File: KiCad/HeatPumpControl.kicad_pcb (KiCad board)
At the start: 2 copper layers, 34.3 x 40.9 mm, 34 parts, among them J1 Conn_01x04_Male, J2 Conn_01x04_Male, J3 Conn_01x04_Male, Q1 2N2222A, U1 TSOP23xx, U2 SeedStudio XIAO ESP32 C3 v1

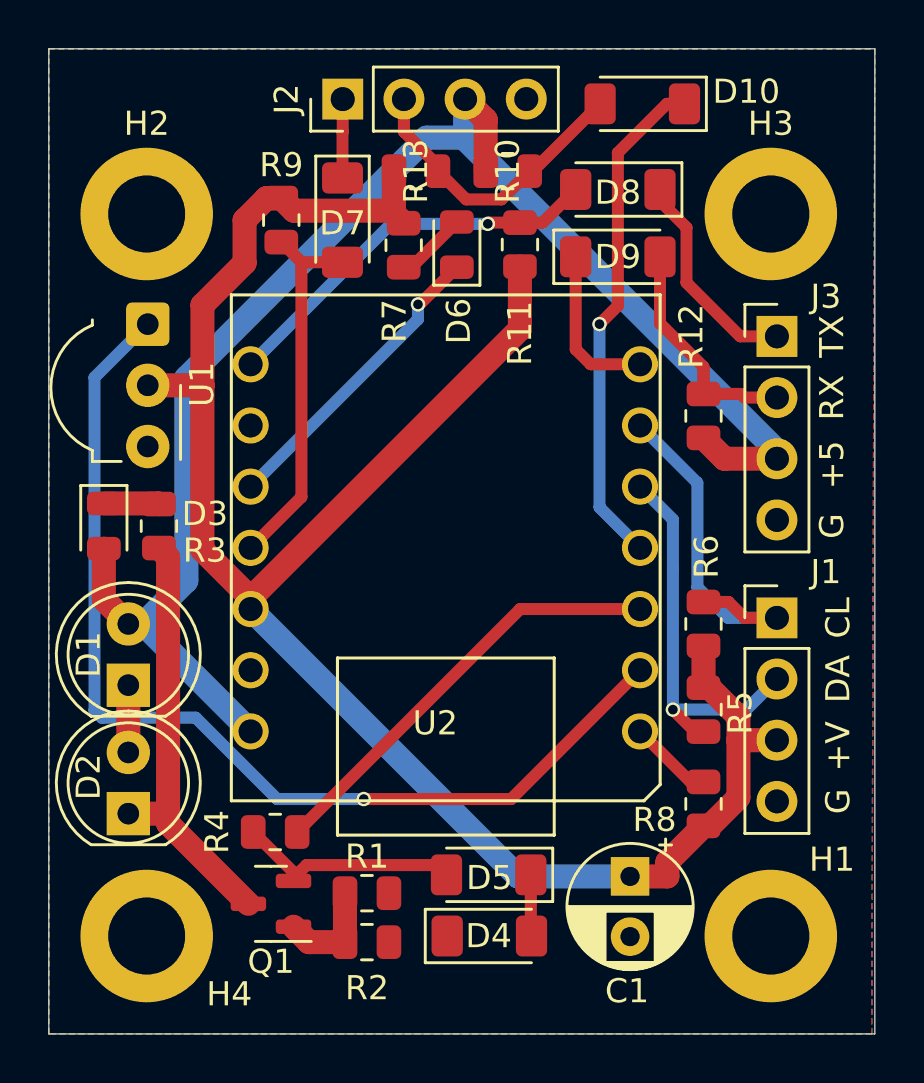
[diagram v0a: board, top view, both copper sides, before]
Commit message: Fixed Q1 pinout and grounding fills
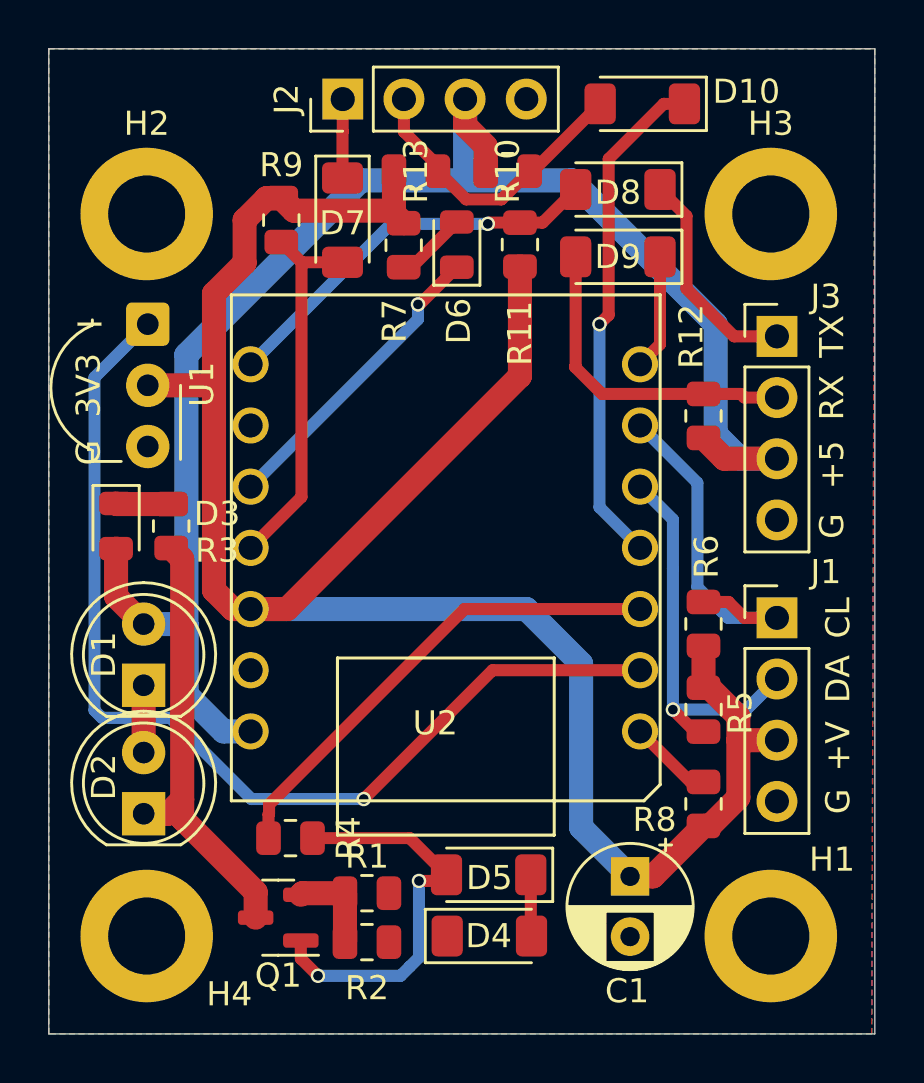
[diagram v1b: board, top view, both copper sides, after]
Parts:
- R1, R2: value 10 -> 27
- R3: value 1.8k -> 470
- R7: value 4k7 -> 430
- moved R4 0.68 mm to (145.9, 134.7), turned to 0 degrees
- moved Q1 0.65 mm to (145.4, 138.0)
- moved D1 0.64 mm to (139.8, 128.4)
- moved D2 0.64 mm to (139.8, 133.7)
- moved D3 0.51 mm to (138.7, 121.8)
- moved R3 0.51 mm to (141.0, 121.8)
- turned D9 to 180 degrees
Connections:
- net Net-(D10-K) renamed /GPIO5
- net Net-(D6-K) renamed /GPIO9
- net Net-(D7-A) renamed /GPIO10
- net Net-(U1-OUT) renamed /GPIO3
- net Net-(U2-IO4/A2/D2) renamed /GPIO4
- D8 pad 1: /TX -> Net-(D8-K)
- D8 pad 2: Net-(D8-A) -> /RX
- D9 pad 1: Net-(D9-K) -> /TX
- D9 pad 2: /RX -> Net-(D9-A)
- J3 pad 1: /TX -> Net-(D8-K)
- J3 pad 2: /RX -> Net-(D9-A)
- Q1 pad 1: /LED1 -> Net-(D4-A)
- Q1 pad 2: Net-(D4-A) -> /LED1
- R11 pad 2: Net-(D8-A) -> /RX
- R12 pad 2: /RX -> Net-(D9-A)
- U2 pad 7: Net-(D9-K) -> /TX
- U2 pad 8: Net-(D8-A) -> /RX
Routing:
- net Net-(D8-A): track 16.5 -> 0.00 mm, vias 1 -> 0
- net Net-(D9-A): track 0.00 -> 13.5 mm
- net Net-(D8-K): track 0.00 -> 9.15 mm
- net Net-(D4-A): track 9.40 -> 16.9 mm, vias 0 -> 2
- net /RX: track 9.55 -> 16.5 mm, vias 0 -> 1
- net Net-(D9-K): track 6.77 -> 0.00 mm
- net +5V: track 64.2 -> 70.8 mm
- net +3V3: track 82.7 -> 88.2 mm
- net /TX: track 9.00 -> 4.80 mm
- net /GPIO4: track 18.1 -> 20.2 mm
- net /LED2: track 18.0 -> 18.6 mm
- net /LED1: track 4.43 -> 3.89 mm
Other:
- board text added: "3V3"
- board text added: "Heat pump controller rev 2.0.1 (C) 2023 - Hans Rune Bue <email@hansrune.net>"
- board text removed: "Heat pump controller rev 2.0 (C) 2023 - Hans Rune Bue <email@hansrune.net>"

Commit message: v2.0.1 KiCAD changes
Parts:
- turned D9 to 0 degrees
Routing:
- net Net-(D9-A): track 13.5 -> 9.55 mm
- net /TX: track 4.80 -> 6.40 mm
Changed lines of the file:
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@@
 		)
 		(property "Value" "1.2k"
-			(at 0 1.65 360)
+			(at 0 1.65 0)
 			(layer "F.Fab")
 			(effects
@@
 		)
 		(property "Footprint" "Resistor_SMD:R_0805_2012Metric"
-			(at 0 0 360)
+			(at 0 0 0)
 			(layer "F.Fab")
 			(hide yes)
@@
 		)
 		(property "Datasheet" ""
-			(at 0 0 360)
+			(at 0 0 0)
 			(layer "F.Fab")
 			(hide yes)
@@
 		)
 		(property "Description" ""
-			(at 0 0 360)
+			(at 0 0 0)
 			(layer "F.Fab")
 			(hide yes)
@@
 		)
 		(fp_text user "${REFERENCE}"
-			(at 0 0 360)
+			(at 0 0 0)
 			(layer "F.Fab")
 			(effects
@@
 	(footprint "Diode_SMD:D_MiniMELF"
 		(layer "F.Cu")
-		(at 159.512 110.617 180)
+		(at 159.512 110.617)
 		(descr "Diode Mini-MELF (SOD-80)")
 		(tags "Diode Mini-MELF (SOD-80)")
@@
 		(attr smd)
 		(fp_line
-			(start 1.75 -1.11)
-			(end -2.66 -1.11)
+			(start -2.66 -1.11)
+			(end -2.66 1.11)
 			(stroke
 				(width 0.12)
@@
 		)
 		(fp_line
-			(start -2.66 -1.11)
-			(end -2.66 1.11)
+			(start 1.75 -1.11)
+			(end -2.66 -1.11)
 			(stroke
 				(width 0.12)
@@
 		)
 		(fp_line
-			(start 2.65 1.1)
-			(end -2.65 1.1)
+			(start -2.65 -1.1)
+			(end 2.65 -1.1)
 			(stroke
 				(width 0.05)
@@
 		)
 		(fp_line
-			(start 2.65 -1.1)
-			(end 2.65 1.1)
+			(start -2.65 1.1)
+			(end -2.65 -1.1)
 			(stroke
 				(width 0.05)
@@
 		)
 		(fp_line
-			(start -2.65 1.1)
-			(end -2.65 -1.1)
+			(start 2.65 -1.1)
+			(end 2.65 1.1)
 			(stroke
 				(width 0.05)
@@
 		)
 		(fp_line
-			(start -2.65 -1.1)
-			(end 2.65 -1.1)
+			(start 2.65 1.1)
+			(end -2.65 1.1)
 			(stroke
 				(width 0.05)
@@
 		)
 		(fp_line
-			(start 1.65 0.8)
-			(end -1.65 0.8)
+			(start -1.65 -0.8)
+			(end 1.65 -0.8)
 			(stroke
 				(width 0.1)
@@
 		)
 		(fp_line
-			(start 1.65 -0.8)
-			(end 1.65 0.8)
+			(start -1.65 0.8)
+			(end -1.65 -0.8)
 			(stroke
 				(width 0.1)
@@
 		)
 		(fp_line
-			(start 0.25 0.4)
+			(start -0.75 0)
 			(end -0.35 0)
 			(stroke
@@
 		)
 		(fp_line
-			(start 0.25 0)
-			(end 0.75 0)
+			(start -0.35 0)
+			(end -0.35 -0.55)
 			(stroke
 				(width 0.1)
@@
 		)
 		(fp_line
-			(start 0.25 -0.4)
-			(end 0.25 0.4)
+			(start -0.35 0)
+			(end -0.35 0.55)
 			(stroke
 				(width 0.1)
@@
 		)
 		(fp_line
-			(start -0.35 0)
-			(end -0.35 0.55)
+			(start 0.25 -0.4)
+			(end 0.25 0.4)
 			(stroke
 				(width 0.1)
@@
 		)
 		(fp_line
-			(start -0.35 0)
-			(end -0.35 -0.55)
+			(start 0.25 0)
+			(end 0.75 0)
 			(stroke
 				(width 0.1)
@@
 		)
 		(fp_line
-			(start -0.75 0)
+			(start 0.25 0.4)
 			(end -0.35 0)
 			(stroke
@@
 		)
 		(fp_line
-			(start -1.65 0.8)
-			(end -1.65 -0.8)
+			(start 1.65 -0.8)
+			(end 1.65 0.8)
 			(stroke
 				(width 0.1)
@@
 		)
 		(fp_line
-			(start -1.65 -0.8)
-			(end 1.65 -0.8)
+			(start 1.65 0.8)
+			(end -1.65 0.8)
 			(stroke
 				(width 0.1)
@@
 		)
 		(pad "1" smd roundrect
-			(at -1.75 0 180)
+			(at -1.75 0)
 			(size 1.3 1.7)
 			(layers "F.Cu" "F.Paste" "F.Mask")
@@
 		)
 		(pad "2" smd roundrect
-			(at 1.75 0 180)
+			(at 1.75 0)
 			(size 1.3 1.7)
 			(layers "F.Cu" "F.Paste" "F.Mask")
@@
 	)
 	(segment
-		(start 161.262 114.249)
+		(start 159.0197 115.0777)
 		(end 160.4333 115.0777)
 		(width 0.5)
@@
 	)
 	(segment
-		(start 161.262 110.617)
-		(end 161.262 114.249)
+		(start 157.762 113.82)
+		(end 159.0197 115.0777)
+		(width 0.5)
+		(layer "F.Cu")
+		(net 17)
+	)
+	(segment
+		(start 157.762 110.617)
+		(end 157.762 113.82)
 		(width 0.5)
 		(layer "F.Cu")
@@
 	)
 	(segment
-		(start 157.762 115.161)
-		(end 157.762 110.617)
+		(start 166.116 116.459)
+		(end 164.766 116.459)
 		(width 0.5)
 		(layer "F.Cu")
@@
 	)
 	(segment
-		(start 163.068 116.3085)
-		(end 158.8535 116.3085)
+		(start 161.262 112.113)
+		(end 163.068 113.919)
 		(width 0.5)
 		(layer "F.Cu")
@@
 	)
 	(segment
-		(start 166.116 116.459)
-		(end 164.766 116.459)
+		(start 163.068 113.919)
+		(end 163.068 116.3085)
 		(width 0.5)
 		(layer "F.Cu")
@@
 	)
 	(segment
-		(start 158.8535 116.3085)
-		(end 157.734 115.189)
+		(start 161.262 110.617)
+		(end 161.262 112.113)
 		(width 0.5)
 		(layer "F.Cu")
@@
 		(width 0.5)
 		(layer "F.Cu")
-		(net 23)
-	)
-	(segment
-		(start 157.734 115.189)
-		(end 157.762 115.161)
-		(width 0.5)
-		(layer "F.Cu")
